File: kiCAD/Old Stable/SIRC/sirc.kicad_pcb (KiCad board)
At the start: 2 copper layers, 55.6 x 40.6 mm, 5 parts, among them IC1 STM8S003F3P, J1 DB25, P1 CONN_01X04

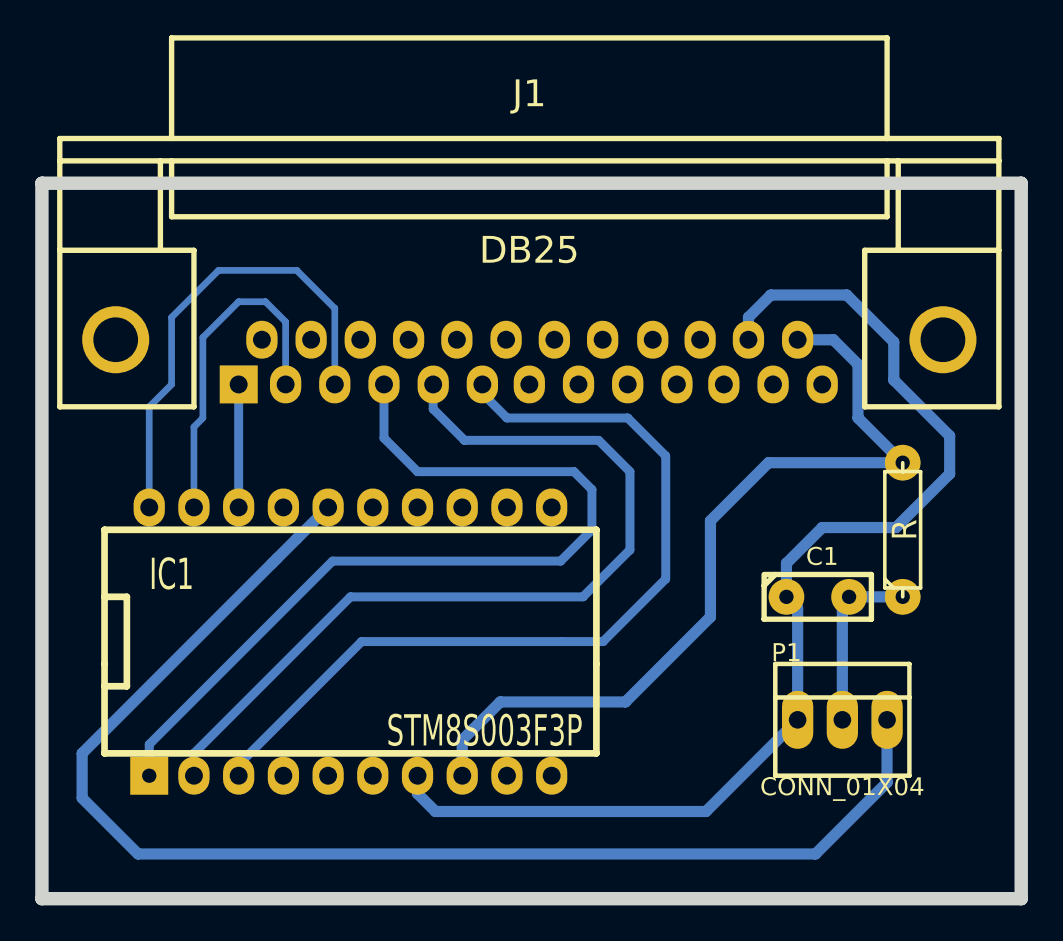
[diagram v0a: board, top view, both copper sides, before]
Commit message: Revision 2, fix DB25 female -> male
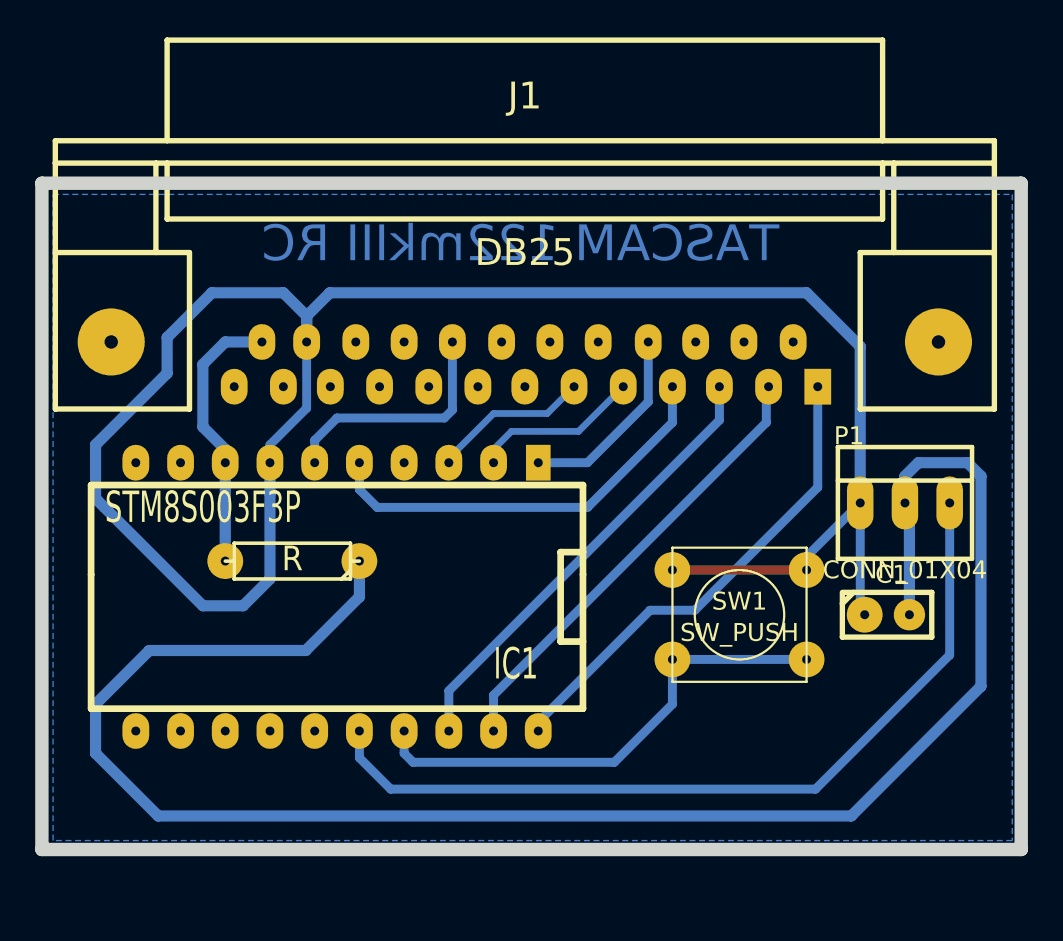
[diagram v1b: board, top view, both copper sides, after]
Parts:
- added SW1: SW_PUSH, SW_PUSH_SMALL, F.Cu at (145.3, 110.2)
- J1: footprint DB25FC -> DB25MC
- moved R1 34.7 mm to (119.9, 107.2), turned to 180 degrees
- moved P1 12.8 mm to (154.7, 103.9)
- moved C1 4.07 mm to (153.7, 110.2)
- moved IC1 2.65 mm to (122.4, 109.2), turned to 180 degrees
- moved J1 0.28 mm to (133.1, 96.0)
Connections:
- IC1 pad 17: (no net) -> N-0000019
- IC1 pad 5: (no net) -> N-0000016
- IC1 pad 6: (no net) -> N-0000018
- J1 pad 1: /CMD0 -> /CMD2
- J1 pad 17: (no net) -> /CMD3
- J1 pad 21: (no net) -> N-0000018
- J1 pad 3: /CMD2 -> /CMD0
- J1 pad 4: /CMD3 -> N-0000016
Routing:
- net N-0000036: track 10.2 -> 173.7 mm
- net GND: track 65.7 -> 112.5 mm
- net /CMD4: track 49.3 -> 9.60 mm
- net /CMD5: track 48.6 -> 9.05 mm
- net /CMD3: track 50.3 -> 11.1 mm
- net VCC: track 47.4 -> 16.3 mm
- net N-0000019: track 0.00 -> 28.2 mm
- net /IR_OUT: track 74.6 -> 47.6 mm
- net N-0000016: track 0.00 -> 23.8 mm
- net /CMD0: track 6.98 -> 25.9 mm
- net N-0000018: track 0.00 -> 13.7 mm
- net /CMD1: track 19.4 -> 26.0 mm
- net /CMD2: track 26.9 -> 27.6 mm
- added copper zone on B.Cu, net GND
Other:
- board size 55.6 x 40.6 mm -> 55.6 x 37.8 mm
- board text added: "TASCAM 122mkIII RC"
